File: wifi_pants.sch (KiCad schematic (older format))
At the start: 26 parts, among them P1 CONN_02X20, P2 CONN_01X10, U1 ESP-12E

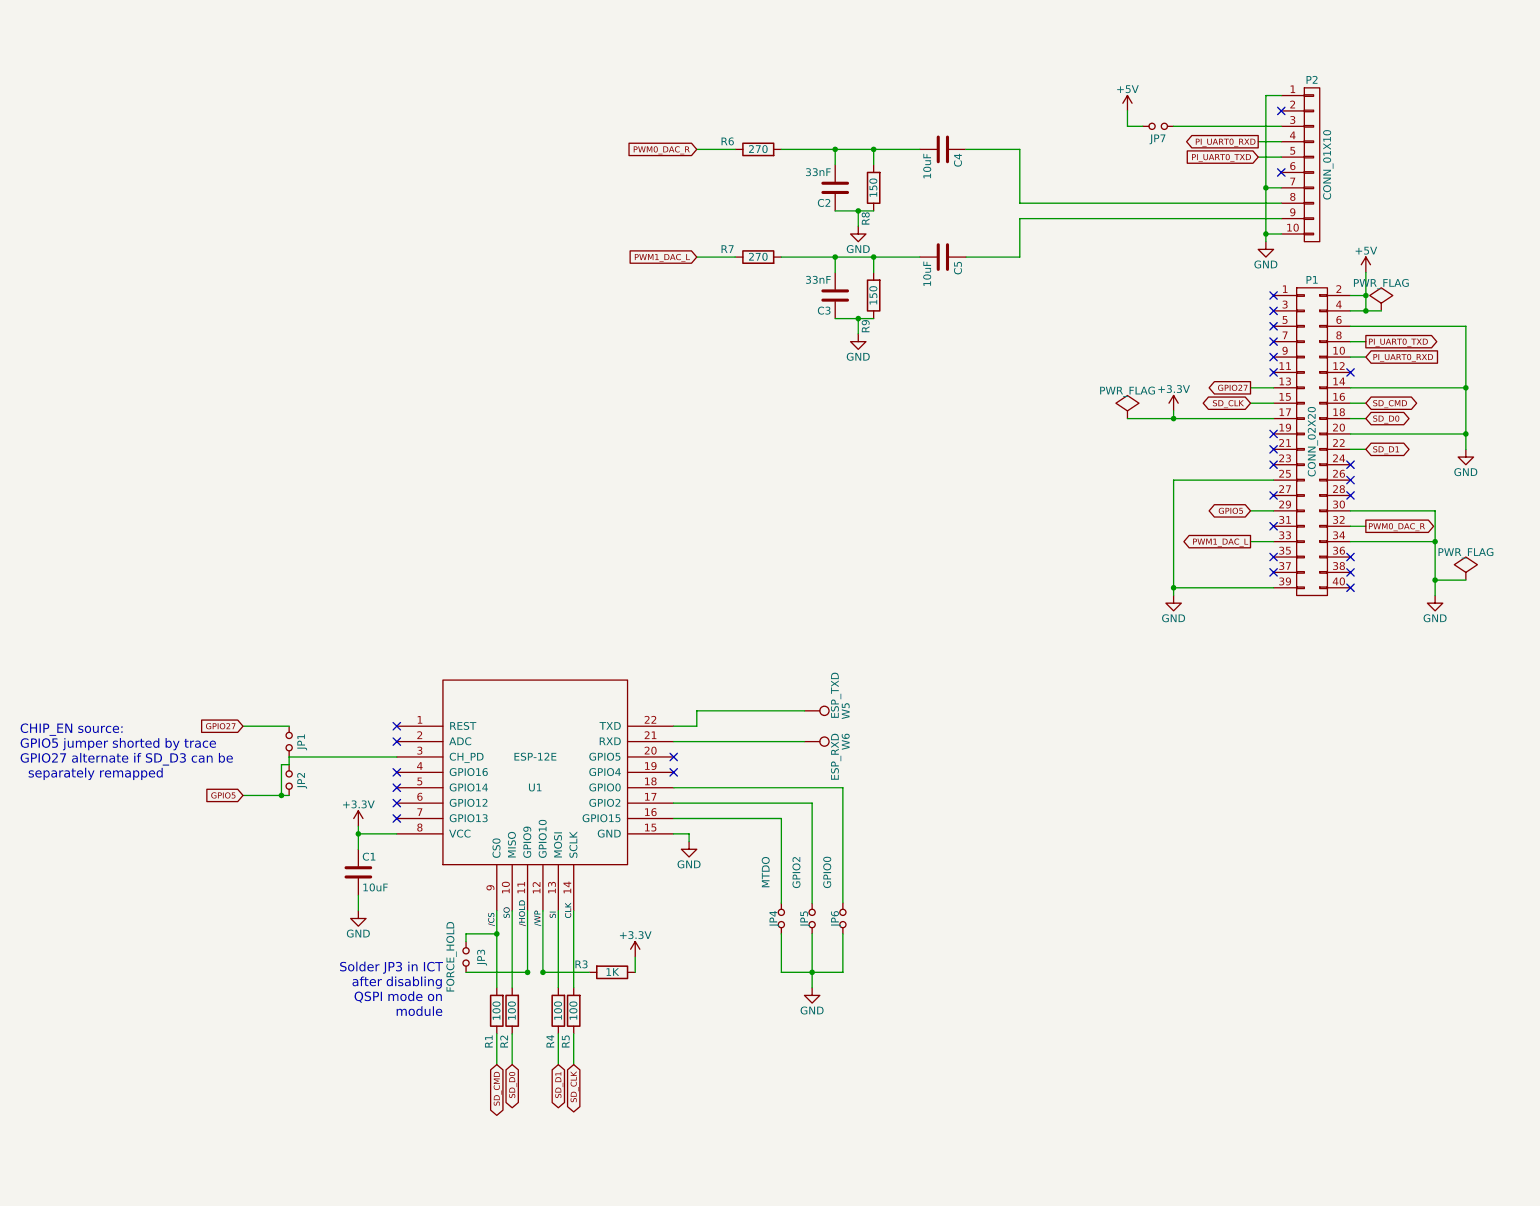
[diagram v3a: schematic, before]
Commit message: r2 schematic and layout
Changes:
-move module antenna offboard to clear the Pi board and components
-SDIO is now routed over a solid ground plane
-remove test points for UART TX/RX on the module.  these can be
 picked off the module topside
-Default to ID_SD as the CHIP_EN default drive.
-Option for full 4 bit SDIO - no guarantees it works though
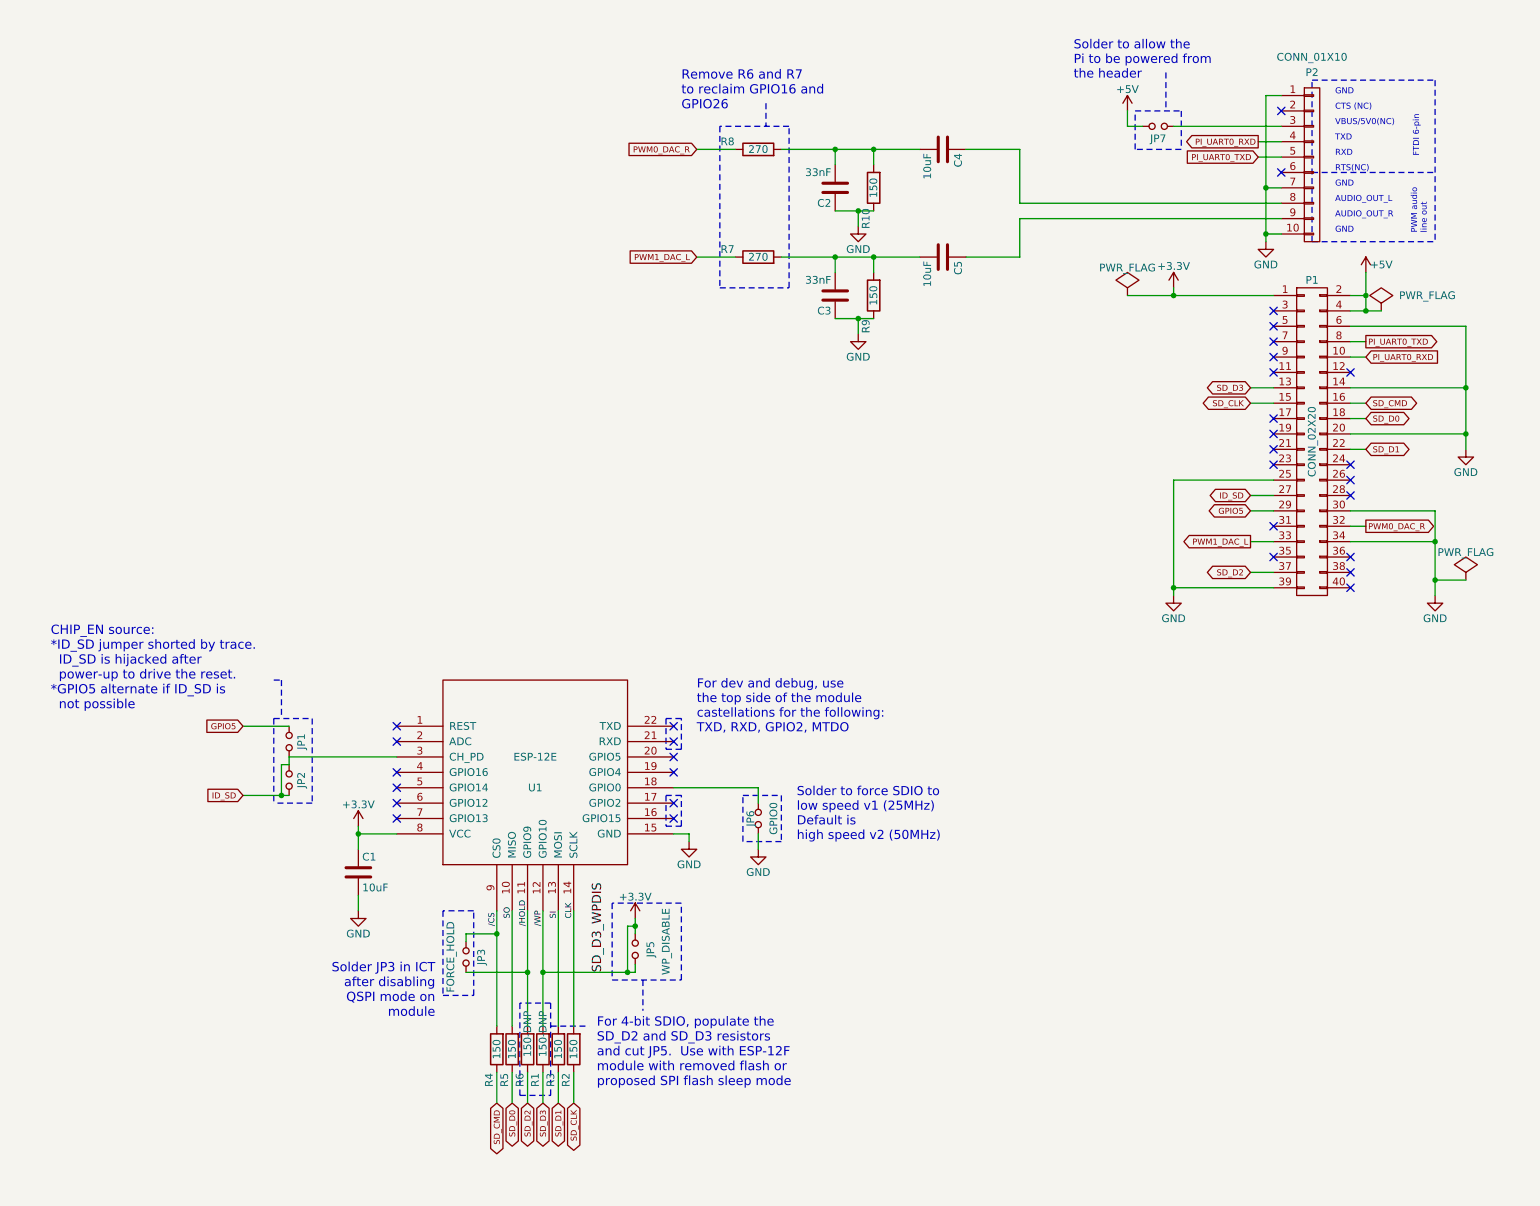
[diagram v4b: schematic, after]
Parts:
- removed JP4: MTDO, wifi_pants:GS2, symbol Jumper_NO_Small
- removed W5: ESP_TXD, wifi_pants:Measurement_Point_Round-SMD-Pad_Small, symbol TEST_1P
- removed W6: ESP_RXD, wifi_pants:Measurement_Point_Round-SMD-Pad_Small, symbol TEST_1P
- added R6: 150-DNP, Resistors_SMD:R_0603_HandSoldering, symbol R
- JP1: value 27 -> GPIO5
- JP2: value 5 -> ID_SD
- JP5: value GPIO2 -> WP_DISABLE
- R1: value 100 -> 150-DNP; Digikey Link http://www.digikey.com/product-detail/en/ERJ-3EKF1000V/P100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 -> http://www.digikey.com/product-detail/en/ERJ-3EKF1500V/P150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; Digikey PN P100HCT-ND -> P150HCT-ND; MFG Part Num ERJ-3EKF1000V -> ERJ-3EKF1500V
- R2, R4, R5: value 100 -> 150; Digikey Link http://www.digikey.com/product-detail/en/ERJ-3EKF1000V/P100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 -> http://www.digikey.com/product-detail/en/ERJ-3EKF1500V/P150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; Digikey PN P100HCT-ND -> P150HCT-ND; MFG Part Num ERJ-3EKF1000V -> ERJ-3EKF1500V
- R3: value 1K -> 150; Digikey Link http://www.digikey.com/product-detail/en/ERJ-3EKF1001V/P1.0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 -> http://www.digikey.com/product-detail/en/ERJ-3EKF1500V/P150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; Digikey PN P1.00KHCT-ND -> P150HCT-ND; MFG Part Num ERJ-3EKF1001V -> ERJ-3EKF1500V
- renumbered R8 to R10, R6 to R8
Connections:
- net +3V3: now also JP5.1, JP5.2, P1.1 (P1), R1.2, U1.12 (GPIO10); no longer P1.17 (P17), R3.1
- net /CS: now also R4.2; no longer R1.2
- net /HOLD: now also R6.2
- net CLK: now also R2.2; no longer R5.2
- net GND: no longer JP5.2
- net GPIO5: now also JP1.1; no longer JP1.2, JP2.1, JP2.2, U1.3 (CH_PD)
- net SD_CLK: now also R2.1; no longer R5.1
- net SD_CMD: now also R4.1; no longer R1.1
- net SD_D0: now also R5.1; no longer R2.1
- net SD_D1: now also R3.1; no longer R4.1
- net SI: now also R3.2; no longer R4.2
- net SO: now also R5.2; no longer R2.2
- net ID_SD: now reaches P1.27 (P27)
- net ID_SD: now also JP1.2, JP2.1, JP2.2, U1.3 (CH_PD)
- net SD_D2: now reaches P1.37 (P37)
- net SD_D2: now also R6.1
- net at U1.17 (GPIO2): no longer JP5.1
- removed net /WP: R3.2, U1.12 (GPIO10)
- net GPIO27 renamed SD_D3
- net SD_D3: now also R1.1; no longer JP1.1
- no-connect marks 30 -> 32
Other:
- note added: "AUDIO_OUT_L"
- note added: "AUDIO_OUT_R"
- note added: "CHIP_EN source:\n*ID_SD jumper shorted by trace.\n ID_SD is hijacked after\n power-up to drive the reset.\n*GPIO5 alternate if ID_SD is\n not possible"
- note added: "CTS (NC)"
- note added: "FTDI 6-pin"
- note added: "For 4-bit SDIO, populate the\nSD_D2 and SD_D3 resistors\nand cut JP5. Use with ESP-12F\nmodule with removed flash or\nproposed SPI flash sleep mode"
- note added: "For dev and debug, use\nthe top side of the module\ncastellations for the following:\nTXD, RXD, GPIO2, MTDO"
- note added: "GND"
- note added: "PWM audio\nline out"
- note added: "RTS(NC)"
- note added: "RXD"
- note added: "Remove R6 and R7\nto reclaim GPIO16 and\nGPIO26"
- note added: "Solder to allow the\nPi to be powered from\nthe header"
- note added: "Solder to force SDIO to\nlow speed v1 (25MHz)\nDefault is\nhigh speed v2 (50MHz)"
- note added: "TXD"
- note added: "VBUS/5V0(NC)"
- note removed: "CHIP_EN source:\nGPIO5 jumper shorted by trace\nGPIO27 alternate if SD_D3 can be\n separately remapped"
- moved on the sheet: JP6

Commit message: Remove audio, place connectors, new 4-bit SDIO routing
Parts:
- removed C2, C3: 33nF, Capacitors_SMD:C_0805_HandSoldering, symbol C
- removed C4, C5: 10uF, Capacitors_SMD:C_0805_HandSoldering, symbol C
- removed JP1: GPIO5, wifi_pants:GS2, symbol Jumper_NO_Small
- removed JP2: ID_SD, wifi_pants:GS2, symbol Jumper_NO_Small
- removed JP3: FORCE_HOLD, wifi_pants:GS2, symbol Jumper_NO_Small
- removed JP5: WP_DISABLE, wifi_pants:GS2, symbol Jumper_NO_Small
- removed JP7: EXT_5V, wifi_pants:GS2, symbol Jumper_NO_Small
- removed R10, R9: 150, Resistors_SMD:R_0603_HandSoldering, symbol R
- removed R7, R8: 270, Resistors_SMD:R_0603_HandSoldering, symbol R
- added P3: CONN_01X02, Connectors_JST_PH:Connectors_JST_S2B-PH-K, symbol CONN_01X02
- C1: footprint Capacitors_SMD:C_0805_HandSoldering -> mcous:0805(2012m)-CHIP-CAP
- P2: value CONN_01X10 -> CONN_01X05; footprint Pin_Headers:Pin_Header_Angled_1x10 -> wifi_pants:Pin_Header_Angled_1x05_mirror; symbol CONN_01X10 -> CONN_01X05; Digikey Link (none) -> http://www.digikey.com/product-detail/en/PRPC005SBAN-M71RC/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; Digikey PN (none) -> S1111EC-05-ND; MFR Name (none) -> Sullins; MFR Part Num (none) -> PRPC005SBAN-M71RC
- R1, R6: value 150-DNP -> 150; footprint Resistors_SMD:R_0603_HandSoldering -> mcous:0603(1608m)-CHIP-RESISTOR
- R2, R3, R4, R5: footprint Resistors_SMD:R_0603_HandSoldering -> mcous:0603(1608m)-CHIP-RESISTOR
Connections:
- net +3V3: no longer R1.2, U1.12 (GPIO10)
- net GND: now also P3.2 (P2); no longer P2.10 (P10), P2.7 (P7)
- net PSU_EN: now reaches P2.2 (P2)
- net PWR_IN: now reaches P2.3 (P3)
- net PWR_IN: now also P3.1 (P1)
- net GPIO5: no longer names the net of P1.29 (P29)
- net PWM0_DAC_R: no longer names the net of P1.32 (P32)
- net PWM1_DAC_L: no longer names the net of P1.33 (P33)
- new net /WP: R1.2, U1.12 (GPIO10)
- no-connect marks 32 -> 34
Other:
- note added: "PSU_EN"
- note added: "PWR_IN"
- note removed: "AUDIO_OUT_L"
- note removed: "AUDIO_OUT_R"
- note removed: "CHIP_EN source:\n*ID_SD jumper shorted by trace.\n ID_SD is hijacked after\n power-up to drive the reset.\n*GPIO5 alternate if ID_SD is\n not possible"
- note removed: "CTS (NC)"
- note removed: "FTDI 6-pin"
- note removed: "For 4-bit SDIO, populate the\nSD_D2 and SD_D3 resistors\nand cut JP5. Use with ESP-12F\nmodule with removed flash or\nproposed SPI flash sleep mode"
- note removed: "PWM audio\nline out"
- note removed: "RTS(NC)"
- note removed: "Remove R6 and R7\nto reclaim GPIO16 and\nGPIO26"
- note removed: "Solder JP3 in ICT\nafter disabling\nQSPI mode on\nmodule\n"
- note removed: "Solder to allow the\nPi to be powered from\nthe header"
- note removed: "VBUS/5V0(NC)"

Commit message: Layout switcher, clean up
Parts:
- added C2, C4, C5: 10uF X5R, mcous:1206(3216m)-CHIP-CAP, symbol C
- added C3: 100pF, mcous:0805(2012m)-CHIP-CAP, symbol C
- added JP1, JP2: Jumper_NO_Small, wifi_pants:GS2, symbol Jumper_NO_Small
- added L1: 2.2uH, wifi_pants:NR6028, symbol INDUCTOR
- added R7, R9: 243K, mcous:0603(1608m)-CHIP-RESISTOR, symbol R
- added R8: 768K, mcous:0603(1608m)-CHIP-RESISTOR, symbol R
- added U2: TPS61252, wifi_pants:WSON-8-1EP_2x2mm_Pitch0.5mm, symbol TPS61252
- P2: value CONN_01X05 -> POWER / UART
- P3: value CONN_01X02 -> JST PH POWER IN
- R1, R2, R3, R4, R5, R6: value 150 -> 33; Digikey Link http://www.digikey.com/product-detail/en/ERJ-3EKF1500V/P150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 -> http://www.digikey.com/product-detail/en/ERJ-3EKF33R0V/P33.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; Digikey PN P150HCT-ND -> P33.0HCT-ND; MFG Part Num ERJ-3EKF1500V -> ERJ-3EKF33R0V
- renumbered JP6 to JP3
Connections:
- net +5V: now also C3.1, C4.1, C5.1, R8.2, U2.2 (VOUT)
- net GND: now also C2.2, C4.2, C5.2, R9.1, U2.1 (GND), U2.4 (ILIM), U2.9 (GND)
- net PWR_IN: now also C2.1, JP2.1, JP2.2, L1.1, R7.2, U2.8 (VIN)
- net PSU_EN renamed /PSU_SHDN
- net /PSU_SHDN: now also JP1.1, JP1.2, R7.1, U2.6 (EN)
- new net: C3.2, R8.1, R9.2, U2.3 (FB)
- new net: L1.2, U2.7 (SW)
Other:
- note added: "/PSU_SHDN"
- note added: "Cut when using the JST\nfor power and an FTDI\ntype cable to prevent\ncontentions with\nCTS (pin 2) and\nUSB VBUS (pin 3)"
- note added: "Must be >13uF after\nDC bias derating at 5v"
- note removed: "PSU_EN"
- moved on the sheet: P3
